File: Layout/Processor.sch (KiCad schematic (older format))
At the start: 9 parts, among them J5 Conn_01x02_Female, J6 Conn_01x02_Female, SW1 SW_Push, U1 DSPIC33FJ128MC804

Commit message: Layout
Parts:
- removed J5: Conn_01x02_Female, Connector_PinSocket_2.54mm:PinSocket_1x02_P2.54mm_Vertical, symbol Connector:Conn_01x02_Female
- added J5: Conn_01x01_Female, Connector_PinSocket_2.54mm:PinSocket_1x01_P2.54mm_Vertical, symbol Connector:Conn_01x01_Female
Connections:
- net RX: now also J5.1 (Pin_1)
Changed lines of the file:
@@
 	5600 5500 5600 5400
-$Comp
-L Connector:Conn_01x02_Female J5
-U 1 1 5F5B5019
-P 9650 2750
-F 0 "J5" H 9678 2726 50  0000 L CNN
-F 1 "Conn_01x02_Female" H 9678 2635 50  0000 L CNN
-F 2 "Connector_PinSocket_2.54mm:PinSocket_1x02_P2.54mm_Vertical" H 9650 2750 50  0001 C CNN
-F 3 "~" H 9650 2750 50  0001 C CNN
-	1    9650 2750
-	1    0    0    -1
-$EndComp
 $Comp
 L Connector:Conn_01x02_Female J6
@@
 $EndComp
 Wire Wire Line
-	9450 2750 9150 2750
-Wire Wire Line
-	9450 2850 9150 2850
-Wire Wire Line
 	9450 3200 9150 3200
 Wire Wire Line
 	9450 3300 9150 3300
-Text GLabel 9150 2750 0    50   Input ~ 0
+Text GLabel 9350 2500 0    50   Input ~ 0
 RX
-Text GLabel 9150 2850 0    50   Input ~ 0
-TX
 Text GLabel 9150 3200 0    50   Input ~ 0
 SCL
 Text GLabel 9150 3300 0    50   Input ~ 0
 SDA
+$Comp
+L Connector:Conn_01x01_Female J5
+U 1 1 5F729F19
+P 9650 2500
+F 0 "J5" H 9678 2526 50  0000 L CNN
+F 1 "Conn_01x01_Female" H 9678 2435 50  0000 L CNN
+F 2 "Connector_PinSocket_2.54mm:PinSocket_1x01_P2.54mm_Vertical" H 9650 2500 50  0001 C CNN
+F 3 "~" H 9650 2500 50  0001 C CNN
+	1    9650 2500
+	1    0    0    -1
+$EndComp
+Wire Wire Line
+	9350 2500 9450 2500
 $EndSCHEMATC

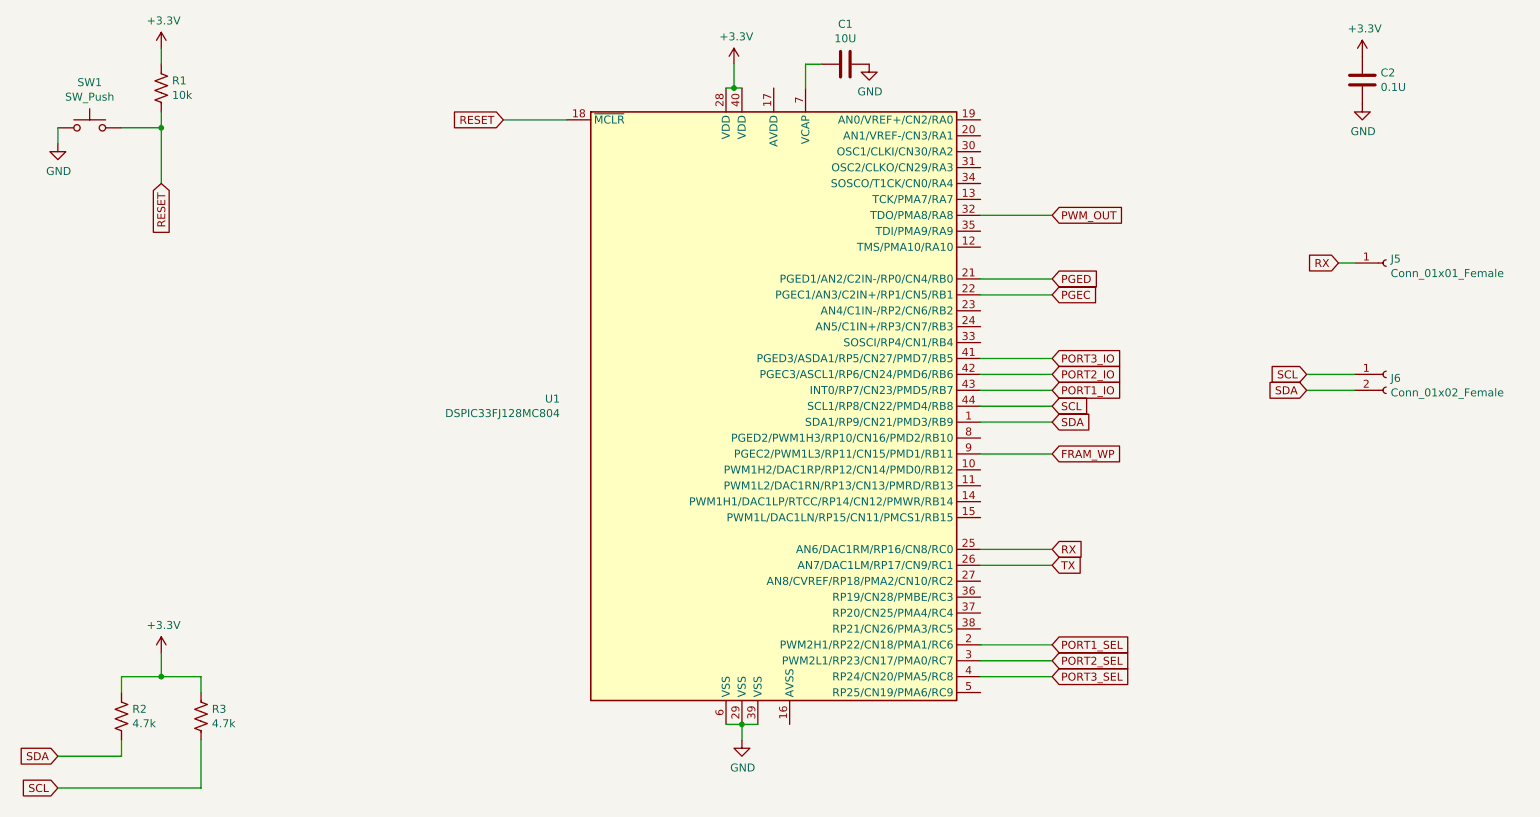
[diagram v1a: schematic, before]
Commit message: Update schematic for new processor
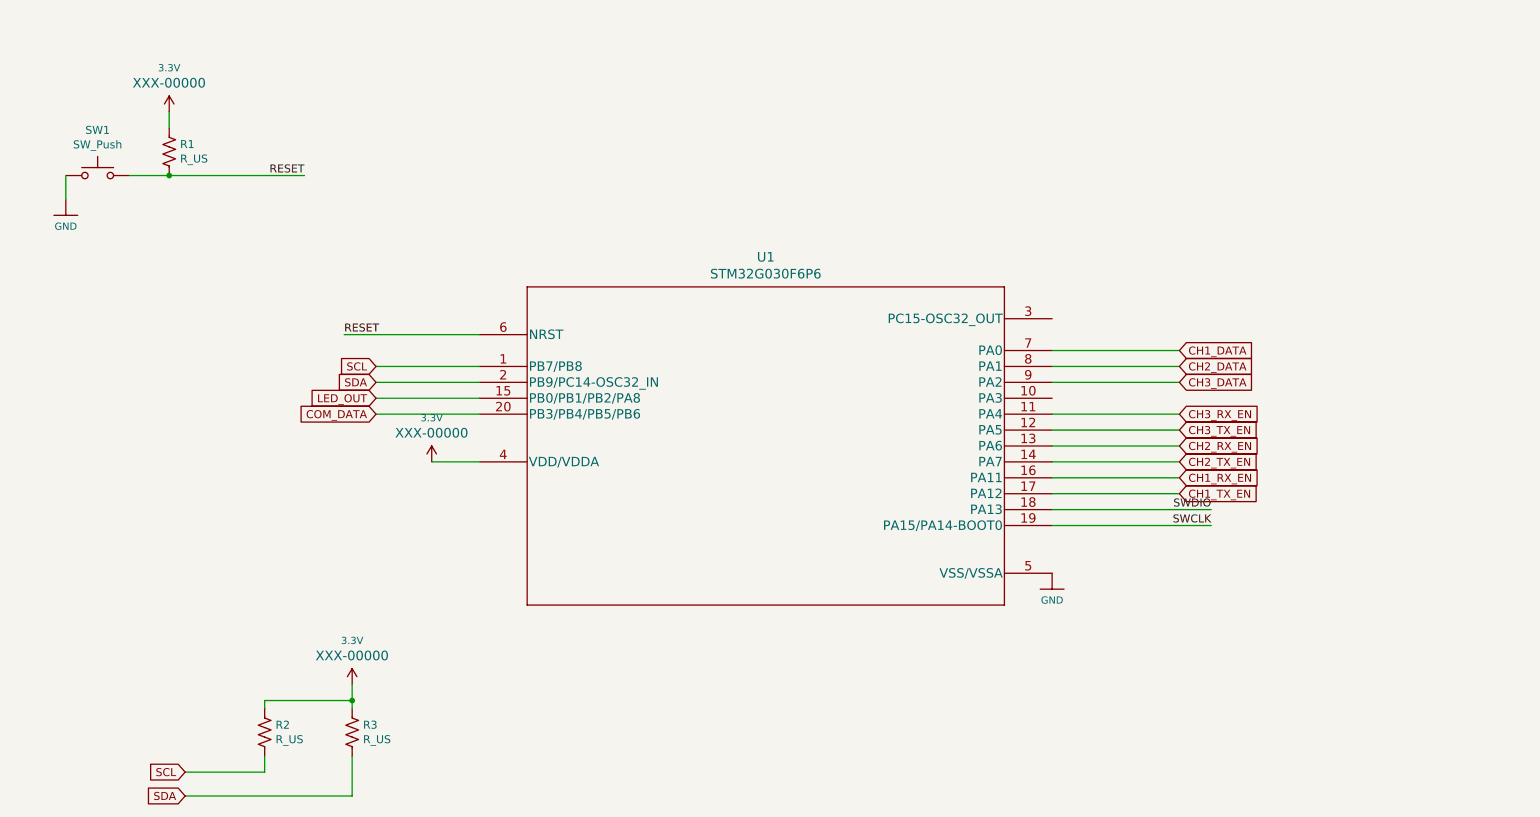
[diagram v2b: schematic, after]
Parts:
- removed C1: 10U, Capacitor_SMD:C_0603_1608Metric_Pad1.05x0.95mm_HandSolder, symbol Device:C
- removed C2: 0.1U, Capacitor_SMD:C_0603_1608Metric_Pad1.05x0.95mm_HandSolder, symbol Device:C
- removed J5: Conn_01x01_Female, Connector_PinSocket_2.54mm:PinSocket_1x01_P2.54mm_Vertical, symbol Connector:Conn_01x01_Female
- removed J6: Conn_01x02_Female, Connector_PinSocket_2.54mm:PinSocket_1x02_P2.54mm_Vertical, symbol Connector:Conn_01x02_Female
- removed U1: DSPIC33FJ128MC804, Package_QFP:TQFP-44_10x10mm_P0.8mm, symbol DSP_Microchip_DSPIC33:DSPIC33FJ128MC804
- added U1: STM32G030F6P6, stm32g030f6p6:STM32G030F6P6, symbol stm32g030f6p6:STM32G030F6P6
- R1: value 10k -> R_US
- R2, R3: value 4.7k -> R_US
- SW1: footprint Button_Switch_SMD:SW_SPST_TL3342 -> Switches:TACTILE_SWITCH_SMD_5.2MM
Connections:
- net GND: now also U1.5 (VSS/VSSA)
- net RESET: now also U1.6 (NRST)
- net SCL: now also R2.2, U1.1 (PB7/PB8); no longer R3.2
- net SDA: now also R3.2, U1.2 (PB9/PC14-OSC32_IN); no longer R2.2
- net +3V3 renamed 3.3V
- net 3.3V: now also U1.4 (VDD/VDDA)
- new net CH1_DATA: U1.7 (PA0)
- new net CH1_RX_EN: U1.16 (PA11)
- new net CH1_TX_EN: U1.17 (PA12)
- new net CH2_DATA: U1.8 (PA1)
- new net CH2_RX_EN: U1.13 (PA6)
- new net CH2_TX_EN: U1.14 (PA7)
- new net CH3_DATA: U1.9 (PA2)
- new net CH3_RX_EN: U1.11 (PA4)
- new net CH3_TX_EN: U1.12 (PA5)
- new net COM_DATA: U1.20 (PB3/PB4/PB5/PB6)
- new net LED_OUT: U1.15 (PB0/PB1/PB2/PA8)
- new net SWCLK: U1.19 (PA15/PA14-BOOT0)
- new net SWDIO: U1.18 (PA13)
